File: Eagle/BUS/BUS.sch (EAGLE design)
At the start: 62 parts

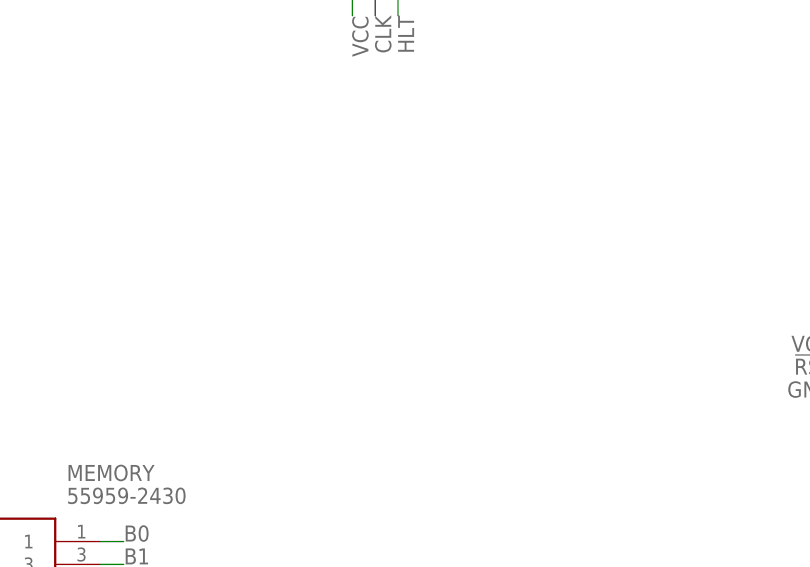
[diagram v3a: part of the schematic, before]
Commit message: added power connector
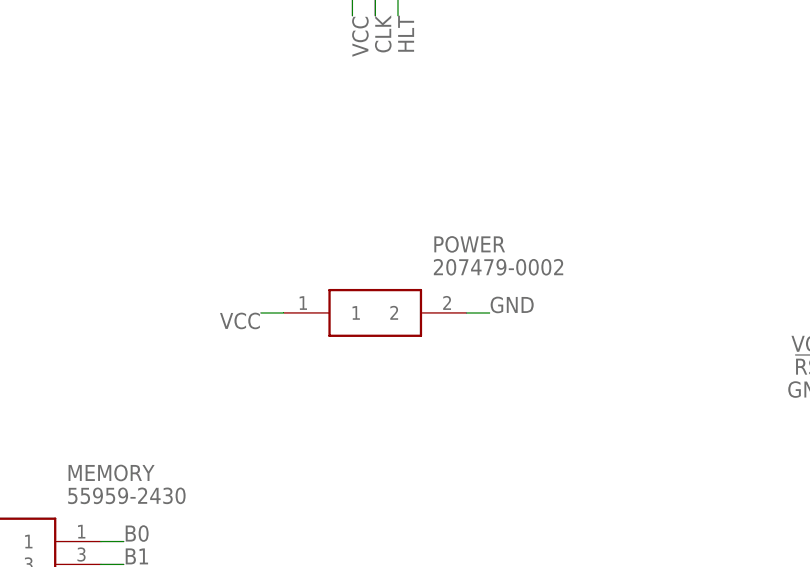
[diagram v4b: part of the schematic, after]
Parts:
- added POWER: 207479-0002, SamacSys_Parts:207479-0002
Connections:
- net GND: now also POWER.2
- net VCC: now also POWER.1
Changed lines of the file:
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@@
 <part name="OR_GATE" library="SamacSys_Parts" deviceset="SN74HC32N" device=""/>
 <part name="FLYBACK_DIODE" library="diode" library_urn="urn:adsk.eagle:library:210" deviceset="1N4148" device="DO35-7" package3d_urn="urn:adsk.eagle:package:43339/2"/>
+<part name="POWER" library="SamacSys_Parts" deviceset="207479-0002" device=""/>
 </parts>
 <sheets>
@@
 <attribute name="VALUE" x="83.5914" y="132.08" size="1.778" layer="96" rot="R90"/>
 </instance>
+<instance part="POWER" gate="G$1" x="2.54" y="170.18" smashed="yes">
+<attribute name="NAME" x="19.05" y="177.8" size="1.778" layer="95" align="center-left"/>
+<attribute name="VALUE" x="19.05" y="175.26" size="1.778" layer="96" align="center-left"/>
+</instance>
 </instances>
 <busses>
@@
 <wire x1="60.96" y1="116.84" x2="63.5" y2="116.84" width="0.1524" layer="91"/>
 <label x="63.5" y="116.84" size="1.778" layer="95"/>
+</segment>
+<segment>
+<pinref part="POWER" gate="G$1" pin="1"/>
+<wire x1="2.54" y1="170.18" x2="0" y2="170.18" width="0.1524" layer="91"/>
+<label x="0" y="170.18" size="1.778" layer="95" rot="R180"/>
 </segment>
 </net>
@@
 <label x="66.04" y="114.3" size="1.778" layer="95"/>
 </segment>
+<segment>
+<pinref part="POWER" gate="G$1" pin="2"/>
+<wire x1="22.86" y1="170.18" x2="25.4" y2="170.18" width="0.1524" layer="91"/>
+<label x="25.4" y="170.18" size="1.778" layer="95"/>
+</segment>
 </net>
